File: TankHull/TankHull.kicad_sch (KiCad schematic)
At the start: 64 parts, among them J1 SlipRing_4, J2 Conn_01x02_Socket, J3 Conn_01x02_Socket, J4 Conn_01x02_Socket, J5 Conn_01x02_Socket, J7 Conn_01x05, Q1 Q_PMOS, U10 TSSP77038TR, U11 TSSP77038TR, U12 TSSP77038TR, U2 DRV8833PWP, U3 DRV8833PWP, U4 TSSP77038TR, U5 TSSP77038TR, U6 TSSP77038TR, U7 TSSP77038TR, U8 PCA9555PW, U9 TSSP77038TR

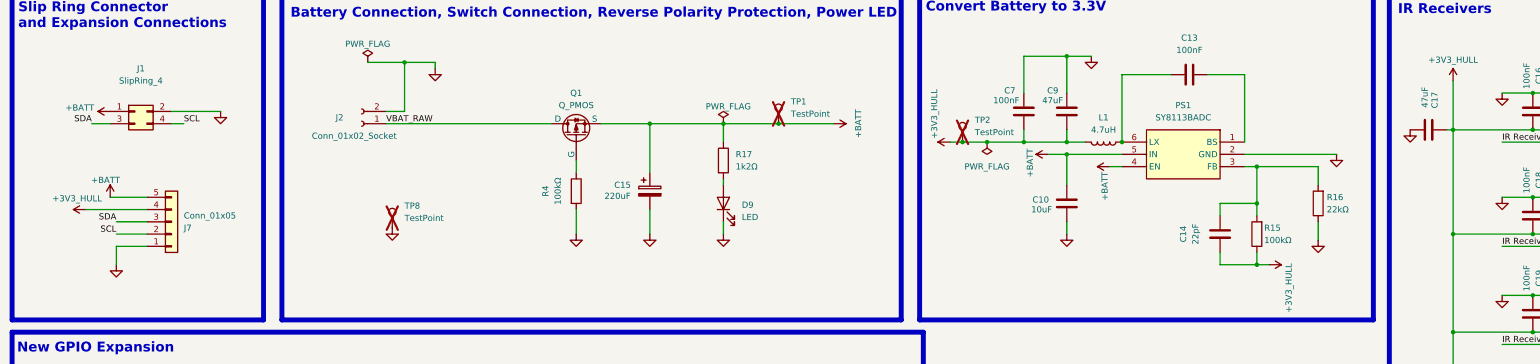
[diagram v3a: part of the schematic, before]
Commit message: submit before using cleanup tool
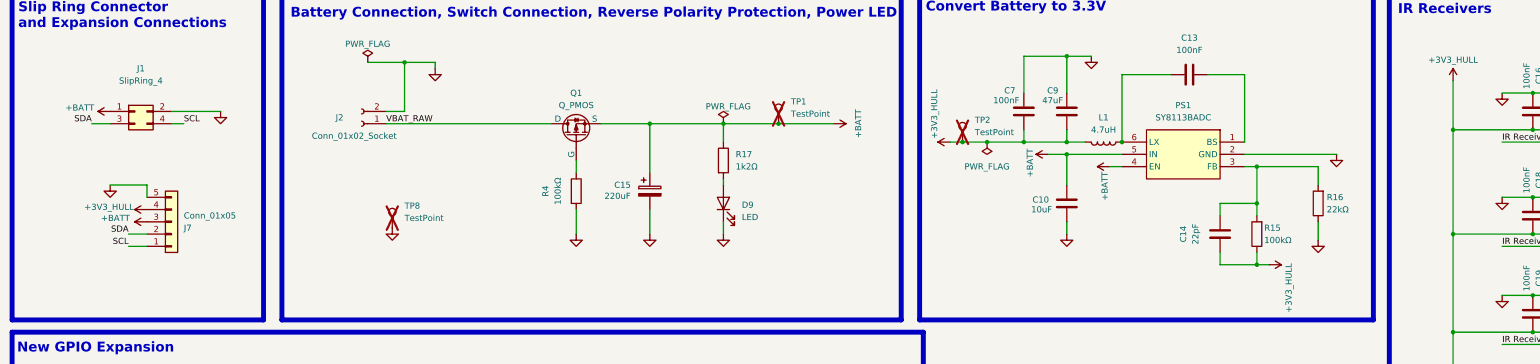
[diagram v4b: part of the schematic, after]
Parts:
- removed C17: 47uF, Capacitor_SMD:C_0805_2012Metric, symbol Device:C
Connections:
- net +BATT: now also J7.3 (Pin_3); no longer J7.5 (Pin_5)
- net GND: now also J7.5 (Pin_5); no longer J7.1 (Pin_1)
- net SCL: now also J7.1 (Pin_1); no longer J7.2 (Pin_2)
- net SDA: now also J7.2 (Pin_2); no longer J7.3 (Pin_3)
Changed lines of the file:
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@@
 	(wire
 		(pts
-			(xy 113.03 219.71) (xy 113.03 209.55)
+			(xy 50.8 64.77) (xy 58.42 64.77)
 		)
 		(stroke
@@
 	(wire
 		(pts
-			(xy 102.87 148.59) (xy 101.6 148.59)
+			(xy 113.03 219.71) (xy 113.03 209.55)
 		)
 		(stroke
@@
 	(wire
 		(pts
-			(xy 50.8 67.31) (xy 58.42 67.31)
+			(xy 102.87 148.59) (xy 101.6 148.59)
 		)
 		(stroke
@@
 	(wire
 		(pts
+			(xy 54.61 77.47) (xy 58.42 77.47)
+		)
+		(stroke
+			(width 0)
+			(type default)
+		)
+	)
+	(wire
+		(pts
 			(xy 88.9 106.68) (xy 88.9 110.49)
 		)
@@
 	(wire
 		(pts
+			(xy 58.42 64.77) (xy 58.42 67.31)
+		)
+		(stroke
+			(width 0)
+			(type default)
+		)
+	)
+	(wire
+		(pts
 			(xy 304.8 58.42) (xy 285.75 58.42)
 		)
@@
 	(wire
 		(pts
-			(xy 52.07 81.28) (xy 52.07 77.47)
-		)
-		(stroke
-			(width 0)
-			(type default)
-		)
-	)
-	(wire
-		(pts
 			(xy 353.06 153.67) (xy 345.44 153.67)
 		)
@@
 	(wire
 		(pts
-			(xy 52.07 74.93) (xy 58.42 74.93)
-		)
-		(stroke
-			(width 0)
-			(type default)
-		)
-	)
-	(wire
-		(pts
 			(xy 101.6 128.27) (xy 176.53 128.27)
 		)
@@
 	(wire
 		(pts
-			(xy 177.8 72.39) (xy 177.8 74.93)
+			(xy 54.61 74.93) (xy 58.42 74.93)
 		)
 		(stroke
@@
 	(wire
 		(pts
-			(xy 213.36 217.17) (xy 209.55 217.17)
+			(xy 177.8 72.39) (xy 177.8 74.93)
 		)
 		(stroke
@@
 	(wire
 		(pts
-			(xy 186.69 246.38) (xy 193.04 246.38)
+			(xy 213.36 217.17) (xy 209.55 217.17)
 		)
 		(stroke
@@
 	(wire
 		(pts
-			(xy 147.32 69.85) (xy 147.32 74.93)
+			(xy 186.69 246.38) (xy 193.04 246.38)
 		)
 		(stroke
@@
 	(wire
 		(pts
-			(xy 186.69 243.84) (xy 193.04 243.84)
+			(xy 147.32 69.85) (xy 147.32 74.93)
 		)
 		(stroke
@@
 	(wire
 		(pts
-			(xy 45.72 69.85) (xy 58.42 69.85)
+			(xy 186.69 243.84) (xy 193.04 243.84)
 		)
 		(stroke
@@
 	(wire
 		(pts
-			(xy 327.66 53.34) (xy 328.93 53.34)
-		)
-		(stroke
-			(width 0)
-			(type default)
-		)
-	)
-	(wire
-		(pts
 			(xy 270.51 41.91) (xy 260.35 41.91)
 		)
@@
 	(wire
 		(pts
-			(xy 52.07 72.39) (xy 58.42 72.39)
-		)
-		(stroke
-			(width 0)
-			(type default)
-		)
-	)
-	(wire
-		(pts
 			(xy 73.66 49.53) (xy 63.5 49.53)
 		)
@@
 	(wire
 		(pts
-			(xy 52.07 77.47) (xy 58.42 77.47)
-		)
-		(stroke
-			(width 0)
-			(type default)
-		)
-	)
-	(wire
-		(pts
 			(xy 92.71 209.55) (xy 97.79 209.55)
 		)
@@
 	)
 	(label "SCL"
-		(at 52.07 74.93 180)
+		(at 54.61 77.47 180)
 		(effects
 			(font
@@
 	)
 	(label "SDA"
-		(at 52.07 72.39 180)
+		(at 54.61 74.93 180)
 		(effects
 			(font
@@
 	)
 	(symbol
-		(lib_id "Device:C")
-		(at 323.85 53.34 90)
-		(unit 1)
-		(exclude_from_sim no)
-		(in_bom yes)
-		(on_board yes)
-		(dnp no)
-		(property "Reference" "C17"
-			(at 325.12 45.466 0)
-			(effects
-				(font
-					(size 1.27 1.27)
-				)
-				(justify right)
-			)
-		)
-		(property "Value" "47uF"
-			(at 323.088 44.45 0)
-			(effects
-				(font
-					(size 1.27 1.27)
-				)
-				(justify right)
-			)
-		)
-		(property "Footprint" "Capacitor_SMD:C_0805_2012Metric"
-			(at 327.66 52.3748 0)
-			(effects
-				(font
-					(size 1.27 1.27)
-				)
-				(hide yes)
-			)
-		)
-		(property "Datasheet" "~"
-			(at 323.85 53.34 0)
-			(effects
-				(font
-					(size 1.27 1.27)
-				)
-				(hide yes)
-			)
-		)
-		(property "Description" "6.3V 47uF X5R ±20% 0805 Multilayer Ceramic Capacitors MLCC - SMD/SMT ROHS"
-			(at 323.85 53.34 0)
-			(effects
-				(font
-					(size 1.27 1.27)
-				)
-				(hide yes)
-			)
-		)
-		(property "JLCPCB Part #" "C16780"
-			(at 325.882 52.324 0)
-			(effects
-				(font
-					(size 1.27 1.27)
-				)
-				(hide yes)
-			)
-		)
-		(property "MANUFACTURER" "Samsung "
-			(at 326.644 55.88 0)
-			(effects
-				(font
-					(size 1.27 1.27)
-				)
-				(hide yes)
-			)
-		)
-		(property "Manufacturer_Part_Number" "C16780"
-			(at 325.882 52.324 0)
-			(effects
-				(font
-					(size 1.27 1.27)
-				)
-				(hide yes)
-			)
-		)
-		(pin "1"
-		)
-		(pin "2"
-		)
-		(instances
-			(project "TankHull"
-				(path "/39d4946a-74a0-412b-8dfb-423b23371da5"
-					(reference "C17")
-					(unit 1)
-				)
-			)
-		)
-	)
-	(symbol
 		(lib_id "power:+BATT")
 		(at 224.79 55.88 90)
@@
 	(symbol
 		(lib_id "power:GND")
-		(at 52.07 81.28 0)
+		(at 50.8 64.77 0)
 		(unit 1)
 		(exclude_from_sim no)
@@
 		(dnp no)
 		(property "Reference" "#PWR027"
-			(at 52.07 87.63 0)
+			(at 50.8 71.12 0)
 			(effects
 				(font
@@
 		)
 		(property "Value" "GND"
-			(at 52.07 86.36 0)
+			(at 50.8 69.85 0)
 			(effects
 				(font
@@
 		)
 		(property "Footprint" ""
-			(at 52.07 81.28 0)
+			(at 50.8 64.77 0)
 			(effects
 				(font
@@
 		)
 		(property "Datasheet" ""
-			(at 52.07 81.28 0)
+			(at 50.8 64.77 0)
 			(effects
 				(font
@@
 		)
 		(property "Description" "Power symbol creates a global label with name \"GND\" , ground"
-			(at 52.07 81.28 0)
+			(at 50.8 64.77 0)
 			(effects
 				(font
@@
 	(symbol
 		(lib_id "power:+BATT")
-		(at 45.72 69.85 90)
+		(at 58.42 69.85 90)
 		(unit 1)
 		(exclude_from_sim no)
@@
 		(dnp no)
 		(property "Reference" "#PWR026"
-			(at 49.53 69.85 0)
+			(at 62.23 69.85 0)
 			(effects
 				(font
@@
 		)
 		(property "Value" "+3V3_HULL"
-			(at 43.942 67.564 90)
+			(at 50.546 69.342 90)
 			(effects
 				(font
@@
 		)
 		(property "Footprint" ""
-			(at 45.72 69.85 0)
+			(at 58.42 69.85 0)
 			(effects
 				(font
@@
 		)
 		(property "Datasheet" ""
-			(at 45.72 69.85 0)
+			(at 58.42 69.85 0)
 			(effects
 				(font
@@
 		)
 		(property "Description" "Power symbol creates a global label with name \"+BATT\""
-			(at 45.72 69.85 0)
+			(at 58.42 69.85 0)
 			(effects
 				(font
@@
 	)
 	(symbol
-		(lib_id "power:GND")
-		(at 320.04 53.34 0)
-		(unit 1)
-		(exclude_from_sim no)
-		(in_bom yes)
-		(on_board yes)
-		(dnp no)
-		(property "Reference" "#PWR049"
-			(at 320.04 59.69 0)
-			(effects
-				(font
-					(size 1.27 1.27)
-				)
-				(hide yes)
-			)
-		)
-		(property "Value" "GND"
-			(at 320.04 58.42 0)
-			(effects
-				(font
-					(size 1.27 1.27)
-				)
-				(hide yes)
-			)
-		)
-		(property "Footprint" ""
-			(at 320.04 53.34 0)
-			(effects
-				(font
-					(size 1.27 1.27)
-				)
-				(hide yes)
-			)
-		)
-		(property "Datasheet" ""
-			(at 320.04 53.34 0)
-			(effects
-				(font
-					(size 1.27 1.27)
-				)
-				(hide yes)
-			)
-		)
-		(property "Description" "Power symbol creates a global label with name \"GND\" , ground"
-			(at 320.04 53.34 0)
-			(effects
-				(font
-					(size 1.27 1.27)
-				)
-				(hide yes)
-			)
-		)
-		(pin "1"
-		)
-		(instances
-			(project "TankHull"
-				(path "/39d4946a-74a0-412b-8dfb-423b23371da5"
-					(reference "#PWR049")
-					(unit 1)
-				)
-			)
-		)
-	)
-	(symbol
 		(lib_id "Device:C")
 		(at 240.03 49.53 180)
@@
 	(symbol
 		(lib_id "power:+BATT")
-		(at 50.8 67.31 0)
-		(mirror y)
+		(at 58.42 72.39 90)
+		(mirror x)
 		(unit 1)
 		(exclude_from_sim no)
@@
 		(dnp no)
 		(property "Reference" "#PWR07"
-			(at 50.8 71.12 0)
+			(at 62.23 72.39 0)
 			(effects
 				(font
@@
 		)
 		(property "Value" "+BATT"
-			(at 52.832 63.754 0)
+			(at 54.864 71.628 90)
 			(effects
 				(font
@@
 		)
 		(property "Footprint" ""
-			(at 50.8 67.31 0)
+			(at 58.42 72.39 0)
 			(effects
 				(font
@@
 		)
 		(property "Datasheet" ""
-			(at 50.8 67.31 0)
+			(at 58.42 72.39 0)
 			(effects
 				(font
@@
 		)
 		(property "Description" "Power symbol creates a global label with name \"+BATT\""
-			(at 50.8 67.31 0)
+			(at 58.42 72.39 0)
 			(effects
 				(font

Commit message: tweaks
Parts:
- removed TP1, TP2: TestPoint, TestPoint:TestPoint_Pad_D1.0mm, symbol Connector:TestPoint
- added C2: 4.7uF, Capacitor_SMD:C_0805_2012Metric, symbol Device:C
- added R1: 47, Resistor_SMD:R_0603_1608Metric, symbol Device:R
- added TP3, TP4, TP5: TestPoint, TestPoint:TestPoint_Pad_D1.0mm, symbol Connector:TestPoint
- R10, R11, R13, R14, R18, R19, R8, R9: JLCPCB Part # C25804 -> C25744; Manufacturer_Part_Number 0603WAF1002T5E -> 0402WGF1002TCE
- U10, U11, U12, U4, U5, U6, U7, U9: value TSSP77038TR -> IRM-V838M3-C/TR1; footprint Vishay IR receiver:TSSP77038TR_VIS -> Everlight IR receiver:XDCR_IRM-V838M3_TR1; symbol Vishay IR Receiver:TSSP77038TR -> Everlight IR Receiver:IRM-V838M3_TR1; Availability (none) -> In Stock; CREATOR (none) -> ANA; Check_prices (none) -> https://www.snapeda.com/parts/IRM-V838M3/TR1/Everlight/view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; Description_1 (none) -> Remote Receiver Sensor 38.0kHz 8m Surface Mount; JLCPCB Part # (none) -> C3291489; MANUFACTURER (none) -> Everlight; MAXIMUM_PACKAGE_HEIGHT (none) -> 3.2mm; MF (none) -> Everlight Electronics Co Ltd; MP (none) -> IRM-V838M3/TR1; Manufacturer_Part_Number (none) -> IRM-V838M3-C/TR1; PARTREV (none) -> 7; Package (none) -> None; Price (none) -> None; Purchase-URL (none) -> https://www.snapeda.com/api/url_track_click_mouser/?unipart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; STANDARD (none) -> Manufacturer Recommendations; SnapEDA_Link (none) -> https://www.snapeda.com/parts/IRM-V838M3/TR1/Everlight/view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; VERIFIER (none) -> RODRIGO
- U8: JLCPCB Part # (none) -> C128392; MANUFACTURER (none) -> NXP Semicon; Manufacturer_Part_Number (none) -> PCA9555PW,118
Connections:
- net +3V3_HULL: now also R1.1; no longer C16.2, U4.2 (VS)
- net GND: now also U10.4 (GND), U11.4 (GND), U12.4 (GND), U4.4 (GND), U5.4 (GND), U6.4 (GND), U7.4 (GND), U9.4 (GND), C2.1; no longer TP8.1
- net IR Receive N: now also TP8.1
- net Left Motor Control 1: now also TP3.1
- net Left Motor Control 2: now also TP4.1
- net Motors Sleep: now also TP5.1
- new net: C16.2, C2.2, R1.2, U4.2 (VCC)
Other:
- moved on the sheet: C16, C18, C19, C20, C22, C23, C24, C25

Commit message: camera connector
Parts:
- added C17, C26, C27, C28, C29, C30, C31: 4.7uF, Capacitor_SMD:C_0805_2012Metric, symbol Device:C
- added R12, R2, R20, R21, R22, R5, R6: 47Ω, Resistor_SMD:R_0603_1608Metric, symbol Device:R
- R1: value 47 -> 47Ω
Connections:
- net +3V3_HULL: now also R12.1, R2.1, R20.1, R21.1, R22.1, R5.1, R6.1; no longer C18.2, C19.2, C20.2, C22.2, C23.2, C24.2, C25.2, U10.2 (VCC), U11.2 (VCC), U12.2 (VCC), U5.2 (VCC), U6.2 (VCC), U7.2 (VCC), U9.2 (VCC)
- net GND: now also C17.1, C26.1, C27.1, C28.1, C30.1
- new net: C19.2, C26.2, R5.2, U6.2 (VCC)
- new net: C17.2, C18.2, R2.2, U5.2 (VCC)
- new net: C20.2, C27.2, R6.2, U12.2 (VCC)
- new net: C23.2, C29.2, R20.2, U10.2 (VCC)
- new net: C25.2, C31.2, R22.2, U7.2 (VCC)
- new net: C22.2, C28.2, R12.2, U11.2 (VCC)
- new net: C24.2, C30.2, R21.2, U9.2 (VCC)
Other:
- moved on the sheet: C19, C20, C22, C23, C24, C25

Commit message: bits
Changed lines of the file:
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@@
 		(on_board yes)
 		(dnp no)
-		(fields_autoplaced yes)
 		(property "Reference" "U8"
 			(at 91.0433 115.57 0)
@@
 		)
 		(property "JLCPCB Part #" "C128392"
-			(at 88.9 143.51 0)
+			(at 85.598 146.05 0)
 			(effects
 				(font
@@
 		)
 		(property "MANUFACTURER" "NXP Semicon "
-			(at 88.9 143.51 0)
+			(at 86.614 144.018 0)
 			(effects
 				(font
@@
 		)
 		(property "Manufacturer_Part_Number" "PCA9555PW,118"
-			(at 88.9 143.51 0)
+			(at 87.63 142.24 0)
 			(effects
 				(font

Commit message: Signed-off-by: SMAUG\Pete <pwbrophy@gmail.com>
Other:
- note added: "Hull: Battery Connection, Switch Connection, Reverse Polarity Protection, Power LED"
- note added: "Hull: Convert Battery to 3.3V"
- note added: "Hull: GPIO Expansion"
- note added: "Hull: IR Receivers"
- note added: "Hull: Left Track and Turret Motor Controller"
- note added: "Hull: Right Track Motor Controller"
- note added: "Hull: Slip Ring Connector and Expansion Connections"
- note removed: "Battery Connection, Switch Connection, Reverse Polarity Protection, Power LED"
- note removed: "Convert Battery to 3.3V"
- note removed: "IR Receivers"
- note removed: "Left Track and Turret Motor Controller"
- note removed: "New GPIO Expansion"
- note removed: "Right Track Motor Controller"
- note removed: "Slip Ring Connector and Expansion Connections"
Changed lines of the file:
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@@
 		)
 	)
-	(text "Left Track and Turret Motor Controller"
+	(text "Hull: Left Track and Turret Motor Controller"
 		(exclude_from_sim no)
 		(at 154.94 184.658 0)
@@
 		)
 	)
-	(text "Convert Battery to 3.3V"
+	(text "Hull: Convert Battery to 3.3V"
 		(exclude_from_sim no)
 		(at 219.71 27.94 0)
@@
 		)
 	)
-	(text "Slip Ring Connector\nand Expansion Connections"
+	(text "Hull: Slip Ring Connector\nand Expansion Connections"
 		(exclude_from_sim no)
 		(at 31.75 29.718 0)
@@
 		)
 	)
-	(text "IR Receivers"
+	(text "Hull: IR Receivers"
 		(exclude_from_sim no)
 		(at 317.5 28.448 0)
@@
 		)
 	)
-	(text "Battery Connection, Switch Connection, Reverse Polarity Protection, Power LED"
+	(text "Hull: Battery Connection, Switch Connection,\nReverse Polarity Protection, Power LED"
 		(exclude_from_sim no)
 		(at 88.138 29.21 0)
@@
 		)
 	)
-	(text "New GPIO Expansion"
+	(text "Hull: GPIO Expansion"
 		(exclude_from_sim no)
 		(at 31.496 98.552 0)
@@
 		)
 	)
-	(text "Right Track Motor Controller"
+	(text "Hull: Right Track Motor Controller"
 		(exclude_from_sim no)
 		(at 31.75 184.658 0)
@@
 	)
 	(junction
-		(at 111.76 39.37)
+		(at 111.76 43.18)
 		(diameter 0)
 		(color 0 0 0 0)
@@
 	(wire
 		(pts
-			(xy 111.76 39.37) (xy 111.76 49.53)
+			(xy 111.76 43.18) (xy 111.76 49.53)
 		)
 		(stroke
@@
 	(wire
 		(pts
-			(xy 118.11 39.37) (xy 118.11 40.64)
+			(xy 118.11 43.18) (xy 118.11 44.45)
 		)
 		(stroke
@@
 	(wire
 		(pts
-			(xy 111.76 39.37) (xy 118.11 39.37)
+			(xy 111.76 43.18) (xy 118.11 43.18)
 		)
 		(stroke
@@
 	(wire
 		(pts
-			(xy 104.14 39.37) (xy 111.76 39.37)
+			(xy 104.14 43.18) (xy 111.76 43.18)
 		)
 		(stroke
@@
 	(symbol
 		(lib_id "power:PWR_FLAG")
-		(at 104.14 39.37 0)
+		(at 104.14 43.18 0)
 		(unit 1)
 		(exclude_from_sim no)
@@
 		(dnp no)
 		(property "Reference" "#FLG01"
-			(at 104.14 37.465 0)
+			(at 104.14 41.275 0)
 			(effects
 				(font
@@
 		)
 		(property "Value" "PWR_FLAG"
-			(at 104.14 35.56 0)
+			(at 104.14 39.37 0)
 			(effects
 				(font
@@
 		)
 		(property "Footprint" ""
-			(at 104.14 39.37 0)
+			(at 104.14 43.18 0)
 			(effects
 				(font
@@
 		)
 		(property "Datasheet" "~"
-			(at 104.14 39.37 0)
+			(at 104.14 43.18 0)
 			(effects
 				(font
@@
 		)
 		(property "Description" "Special symbol for telling ERC where power comes from"
-			(at 104.14 39.37 0)
+			(at 104.14 43.18 0)
 			(effects
 				(font
@@
 	(symbol
 		(lib_id "power:GND")
-		(at 118.11 40.64 0)
+		(at 118.11 44.45 0)
 		(unit 1)
 		(exclude_from_sim no)
@@
 		(fields_autoplaced yes)
 		(property "Reference" "#PWR014"
-			(at 118.11 46.99 0)
+			(at 118.11 50.8 0)
 			(effects
 				(font
@@
 		)
 		(property "Value" "GND"
-			(at 118.11 45.72 0)
+			(at 118.11 49.53 0)
 			(effects
 				(font
@@
 		)
 		(property "Footprint" ""
-			(at 118.11 40.64 0)
+			(at 118.11 44.45 0)
 			(effects
 				(font
@@
 		)
 		(property "Datasheet" ""
-			(at 118.11 40.64 0)
+			(at 118.11 44.45 0)
 			(effects
 				(font
@@
 		)
 		(property "Description" "Power symbol creates a global label with name \"GND\" , ground"
-			(at 118.11 40.64 0)
+			(at 118.11 44.45 0)
 			(effects
 				(font
